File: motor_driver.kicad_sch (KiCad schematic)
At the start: 8 parts, among them J3 Conn_01x06, J4 Conn_01x06, U7 TB6612FNG

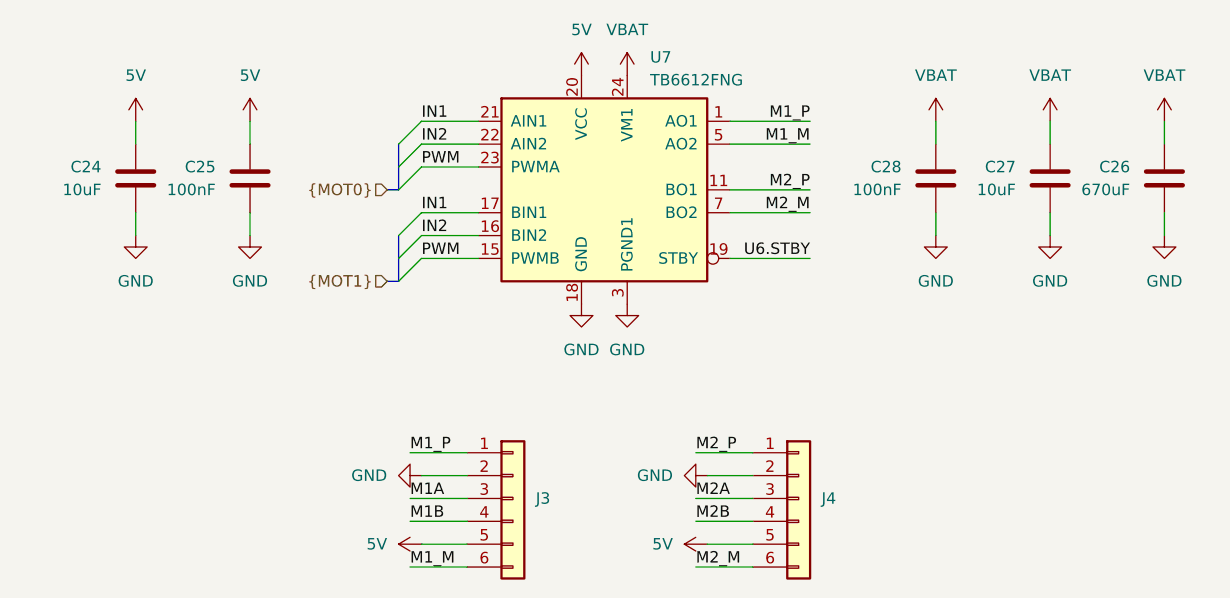
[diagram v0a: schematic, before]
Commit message: Replace schottky with ideal diode
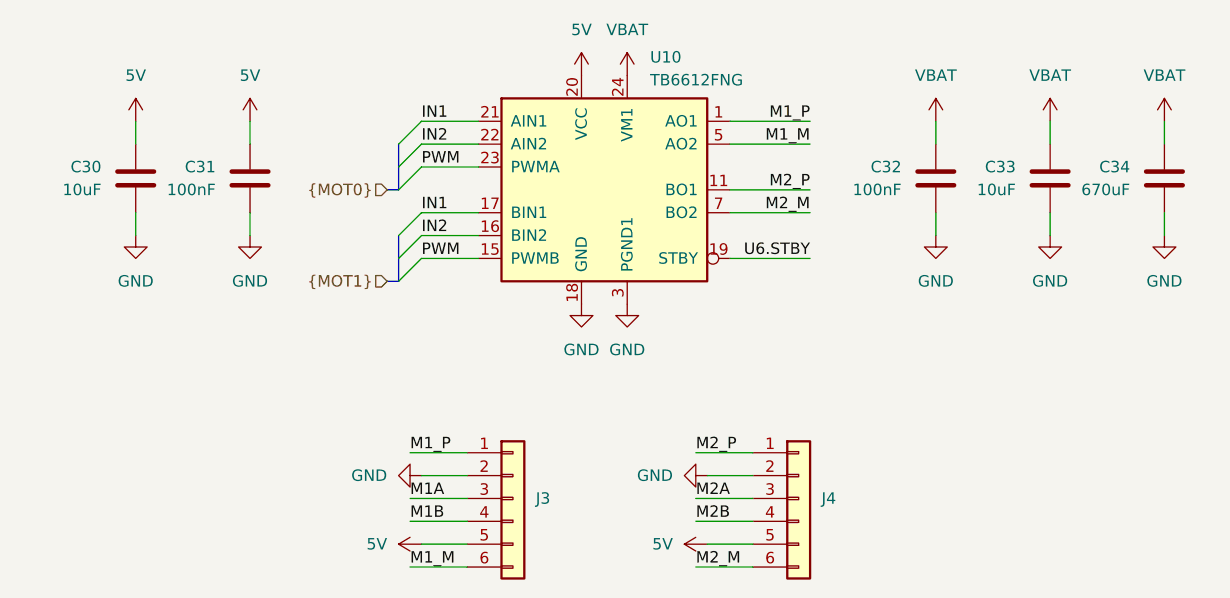
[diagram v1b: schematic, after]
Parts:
- renumbered C24 to C30, C25 to C31, C28 to C32, C27 to C33, C26 to C34, U7 to U10
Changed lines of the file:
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@@
 		(dnp no)
 		(fields_autoplaced yes)
-		(property "Reference" "#PWR082"
+		(property "Reference" "#PWR0103"
 			(at 209.55 83.82 0)
 			(effects
@@
 			(project "Tumbler2_Redesign"
 				(path "/f3fd8d79-9d35-4c04-811e-2697a2740958/f393b342-ddad-47d4-8b4e-f21b64e15add"
-					(reference "#PWR082")
+					(reference "#PWR0103")
 					(unit 1)
 				)
@@
 		(dnp no)
 		(fields_autoplaced yes)
-		(property "Reference" "#PWR083"
+		(property "Reference" "#PWR0112"
 			(at 152.4 119.38 0)
 			(effects
@@
 			(project "Tumbler2_Redesign"
 				(path "/f3fd8d79-9d35-4c04-811e-2697a2740958/f393b342-ddad-47d4-8b4e-f21b64e15add"
-					(reference "#PWR083")
+					(reference "#PWR0112")
 					(unit 1)
 				)
@@
 		(dnp no)
 		(fields_autoplaced yes)
-		(property "Reference" "#PWR076"
+		(property "Reference" "#PWR098"
 			(at 149.86 78.74 0)
 			(effects
@@
 			(project "Tumbler2_Redesign"
 				(path "/f3fd8d79-9d35-4c04-811e-2697a2740958/f393b342-ddad-47d4-8b4e-f21b64e15add"
-					(reference "#PWR076")
+					(reference "#PWR098")
 					(unit 1)
 				)
@@
 		(dnp no)
 		(fields_autoplaced yes)
-		(property "Reference" "#PWR078"
+		(property "Reference" "#PWR099"
 			(at 95.25 83.82 0)
 			(effects
@@
 			(project "Tumbler2_Redesign"
 				(path "/f3fd8d79-9d35-4c04-811e-2697a2740958/f393b342-ddad-47d4-8b4e-f21b64e15add"
-					(reference "#PWR078")
+					(reference "#PWR099")
 					(unit 1)
 				)
@@
 		(dnp no)
 		(fields_autoplaced yes)
-		(property "Reference" "#PWR077"
+		(property "Reference" "#PWR0113"
 			(at 130.81 127 0)
 			(effects
@@
 			(project "Tumbler2_Redesign"
 				(path "/f3fd8d79-9d35-4c04-811e-2697a2740958/f393b342-ddad-47d4-8b4e-f21b64e15add"
-					(reference "#PWR077")
+					(reference "#PWR0113")
 					(unit 1)
 				)
@@
 		(on_board yes)
 		(dnp no)
-		(property "Reference" "C25"
+		(property "Reference" "C31"
 			(at 104.14 85.0899 0)
 			(effects
@@
 			(project "Tumbler2_Redesign"
 				(path "/f3fd8d79-9d35-4c04-811e-2697a2740958/f393b342-ddad-47d4-8b4e-f21b64e15add"
-					(reference "C25")
+					(reference "C31")
 					(unit 1)
 				)
@@
 		(dnp no)
 		(fields_autoplaced yes)
-		(property "Reference" "#PWR079"
+		(property "Reference" "#PWR0100"
 			(at 107.95 83.82 0)
 			(effects
@@
 			(project "Tumbler2_Redesign"
 				(path "/f3fd8d79-9d35-4c04-811e-2697a2740958/f393b342-ddad-47d4-8b4e-f21b64e15add"
-					(reference "#PWR079")
+					(reference "#PWR0100")
 					(unit 1)
 				)
@@
 		(dnp no)
 		(fields_autoplaced yes)
-		(property "Reference" "#PWR089"
+		(property "Reference" "#PWR0114"
 			(at 162.56 127 0)
 			(effects
@@
 			(project "Tumbler2_Redesign"
 				(path "/f3fd8d79-9d35-4c04-811e-2697a2740958/f393b342-ddad-47d4-8b4e-f21b64e15add"
-					(reference "#PWR089")
+					(reference "#PWR0114")
 					(unit 1)
 				)
@@
 		(on_board yes)
 		(dnp no)
-		(property "Reference" "U7"
+		(property "Reference" "U10"
 			(at 152.4 72.898 0)
 			(effects
@@
 			(project "Tumbler2_Redesign"
 				(path "/f3fd8d79-9d35-4c04-811e-2697a2740958/f393b342-ddad-47d4-8b4e-f21b64e15add"
-					(reference "U7")
+					(reference "U10")
 					(unit 1)
 				)
@@
 		(on_board yes)
 		(dnp no)
-		(property "Reference" "C27"
+		(property "Reference" "C33"
 			(at 193.04 85.0899 0)
 			(effects
@@
 			(project "Tumbler2_Redesign"
 				(path "/f3fd8d79-9d35-4c04-811e-2697a2740958/f393b342-ddad-47d4-8b4e-f21b64e15add"
-					(reference "C27")
+					(reference "C33")
 					(unit 1)
 				)
@@
 		(dnp no)
 		(fields_autoplaced yes)
-		(property "Reference" "#PWR085"
+		(property "Reference" "#PWR0105"
 			(at 107.95 99.06 0)
 			(effects
@@
 			(project "Tumbler2_Redesign"
 				(path "/f3fd8d79-9d35-4c04-811e-2697a2740958/f393b342-ddad-47d4-8b4e-f21b64e15add"
-					(reference "#PWR085")
+					(reference "#PWR0105")
 					(unit 1)
 				)
@@
 		(dnp no)
 		(fields_autoplaced yes)
-		(property "Reference" "#PWR090"
+		(property "Reference" "#PWR0109"
 			(at 144.78 106.68 0)
 			(effects
@@
 			(project "Tumbler2_Redesign"
 				(path "/f3fd8d79-9d35-4c04-811e-2697a2740958/f393b342-ddad-47d4-8b4e-f21b64e15add"
-					(reference "#PWR090")
+					(reference "#PWR0109")
 					(unit 1)
 				)
@@
 		(dnp no)
 		(fields_autoplaced yes)
-		(property "Reference" "#PWR074"
+		(property "Reference" "#PWR0111"
 			(at 120.65 119.38 0)
 			(effects
@@
 			(project "Tumbler2_Redesign"
 				(path "/f3fd8d79-9d35-4c04-811e-2697a2740958/f393b342-ddad-47d4-8b4e-f21b64e15add"
-					(reference "#PWR074")
+					(reference "#PWR0111")
 					(unit 1)
 				)
@@
 		(dnp no)
 		(fields_autoplaced yes)
-		(property "Reference" "#PWR080"
+		(property "Reference" "#PWR0101"
 			(at 184.15 83.82 0)
 			(effects
@@
 			(project "Tumbler2_Redesign"
 				(path "/f3fd8d79-9d35-4c04-811e-2697a2740958/f393b342-ddad-47d4-8b4e-f21b64e15add"
-					(reference "#PWR080")
+					(reference "#PWR0101")
 					(unit 1)
 				)
@@
 		(dnp no)
 		(fields_autoplaced yes)
-		(property "Reference" "#PWR088"
+		(property "Reference" "#PWR0108"
 			(at 209.55 99.06 0)
 			(effects
@@
 			(project "Tumbler2_Redesign"
 				(path "/f3fd8d79-9d35-4c04-811e-2697a2740958/f393b342-ddad-47d4-8b4e-f21b64e15add"
-					(reference "#PWR088")
+					(reference "#PWR0108")
 					(unit 1)
 				)
@@
 		(on_board yes)
 		(dnp no)
-		(property "Reference" "C26"
+		(property "Reference" "C34"
 			(at 205.74 85.0899 0)
 			(effects
@@
 			(project "Tumbler2_Redesign"
 				(path "/f3fd8d79-9d35-4c04-811e-2697a2740958/f393b342-ddad-47d4-8b4e-f21b64e15add"
-					(reference "C26")
+					(reference "C34")
 					(unit 1)
 				)
@@
 		(dnp no)
 		(fields_autoplaced yes)
-		(property "Reference" "#PWR087"
+		(property "Reference" "#PWR0107"
 			(at 196.85 99.06 0)
 			(effects
@@
 			(project "Tumbler2_Redesign"
 				(path "/f3fd8d79-9d35-4c04-811e-2697a2740958/f393b342-ddad-47d4-8b4e-f21b64e15add"
-					(reference "#PWR087")
+					(reference "#PWR0107")
 					(unit 1)
 				)
@@
 		(dnp no)
 		(fields_autoplaced yes)
-		(property "Reference" "#PWR086"
+		(property "Reference" "#PWR0106"
 			(at 184.15 99.06 0)
 			(effects
@@
 			(project "Tumbler2_Redesign"
 				(path "/f3fd8d79-9d35-4c04-811e-2697a2740958/f393b342-ddad-47d4-8b4e-f21b64e15add"
-					(reference "#PWR086")
+					(reference "#PWR0106")
 					(unit 1)
 				)
@@
 		(dnp no)
 		(fields_autoplaced yes)
-		(property "Reference" "#PWR075"
+		(property "Reference" "#PWR097"
 			(at 144.78 78.74 0)
 			(effects
@@
 			(project "Tumbler2_Redesign"
 				(path "/f3fd8d79-9d35-4c04-811e-2697a2740958/f393b342-ddad-47d4-8b4e-f21b64e15add"
-					(reference "#PWR075")
+					(reference "#PWR097")
 					(unit 1)
 				)
@@
 		(on_board yes)
 		(dnp no)
-		(property "Reference" "C28"
+		(property "Reference" "C32"
 			(at 180.34 85.0899 0)
 			(effects
@@
 			(project "Tumbler2_Redesign"
 				(path "/f3fd8d79-9d35-4c04-811e-2697a2740958/f393b342-ddad-47d4-8b4e-f21b64e15add"
-					(reference "C28")
+					(reference "C32")
 					(unit 1)
 				)
@@
 		(dnp no)
 		(fields_autoplaced yes)
-		(property "Reference" "#PWR084"
+		(property "Reference" "#PWR0104"
 			(at 95.25 99.06 0)
 			(effects
@@
 			(project "Tumbler2_Redesign"
 				(path "/f3fd8d79-9d35-4c04-811e-2697a2740958/f393b342-ddad-47d4-8b4e-f21b64e15add"
-					(reference "#PWR084")
+					(reference "#PWR0104")
 					(unit 1)
 				)
@@
 		(dnp no)
 		(fields_autoplaced yes)
-		(property "Reference" "#PWR081"
+		(property "Reference" "#PWR0102"
 			(at 196.85 83.82 0)
 			(effects
@@
 			(project "Tumbler2_Redesign"
 				(path "/f3fd8d79-9d35-4c04-811e-2697a2740958/f393b342-ddad-47d4-8b4e-f21b64e15add"
-					(reference "#PWR081")
+					(reference "#PWR0102")
 					(unit 1)
 				)
@@
 		(dnp no)
 		(fields_autoplaced yes)
-		(property "Reference" "#PWR091"
+		(property "Reference" "#PWR0110"
 			(at 149.86 106.68 0)
 			(effects
@@
 			(project "Tumbler2_Redesign"
 				(path "/f3fd8d79-9d35-4c04-811e-2697a2740958/f393b342-ddad-47d4-8b4e-f21b64e15add"
-					(reference "#PWR091")
+					(reference "#PWR0110")
 					(unit 1)
 				)
@@
 		(on_board yes)
 		(dnp no)
-		(property "Reference" "C24"
+		(property "Reference" "C30"
 			(at 91.44 85.0899 0)
 			(effects
@@
 			(project "Tumbler2_Redesign"
 				(path "/f3fd8d79-9d35-4c04-811e-2697a2740958/f393b342-ddad-47d4-8b4e-f21b64e15add"
-					(reference "C24")
-					(unit 1)
-				)
+					(reference "C30")
+					(unit 1)
+				)
